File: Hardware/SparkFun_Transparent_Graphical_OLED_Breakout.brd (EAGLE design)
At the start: 25.4 x 25.4 mm, 61 parts, among them U1 AP3012, U2 UG-2856KLBAG01_4WSPI

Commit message: Add capacitor to reset line for delayed start up!
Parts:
- moved U$10 2.54 mm to (11.4, 1.40)
- moved U$11 2.54 mm to (14.0, 1.27)
- moved U$6 2.54 mm to (14.0, 1.40)
- moved U$7 2.54 mm to (11.4, 1.27)
- moved U$12 2.54 mm to (16.5, 1.40)
- moved U$15 2.54 mm to (16.5, 1.27)
- moved U$8 2.54 mm to (19.1, 1.27)
- moved U$9 2.54 mm to (19.1, 1.52)
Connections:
- net !CS: now also J3.6; no longer J3.5
- net D!C!/SA0: now also J3.5; no longer J3.6
- net SCLK/SCL: now also J3.4; no longer J3.3
- net SDIN/SDA: now also J3.3; no longer J3.4
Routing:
- net !CS: track 35.5 -> 32.1 mm, vias 6 -> 5
- net SDIN/SDA: track 64.3 -> 61.8 mm
- net SCLK/SCL: track 59.1 -> 61.6 mm
- net D!C!/SA0: track 32.4 -> 30.1 mm

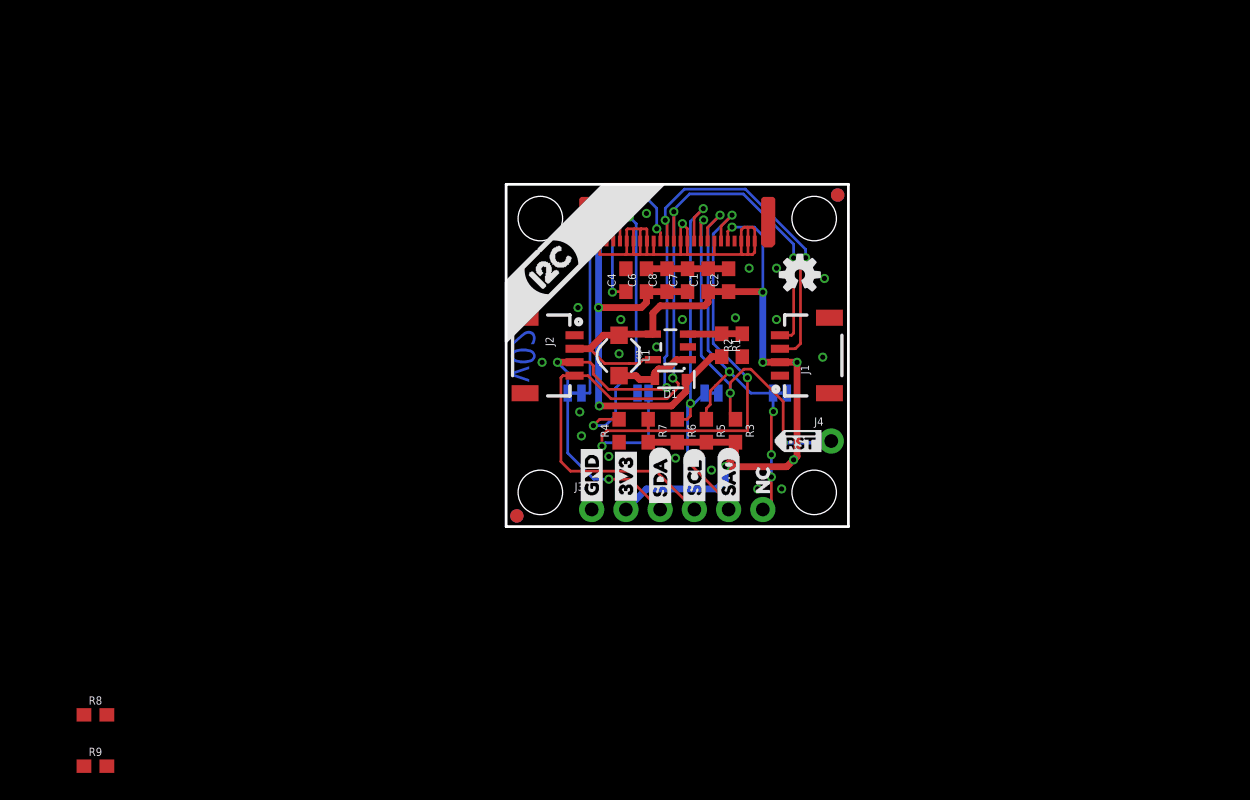
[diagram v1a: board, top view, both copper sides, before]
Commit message: Fixed proto issues
Added I2C pullup resistors and disconnect jumper, added power LED, added reset timing capacitor
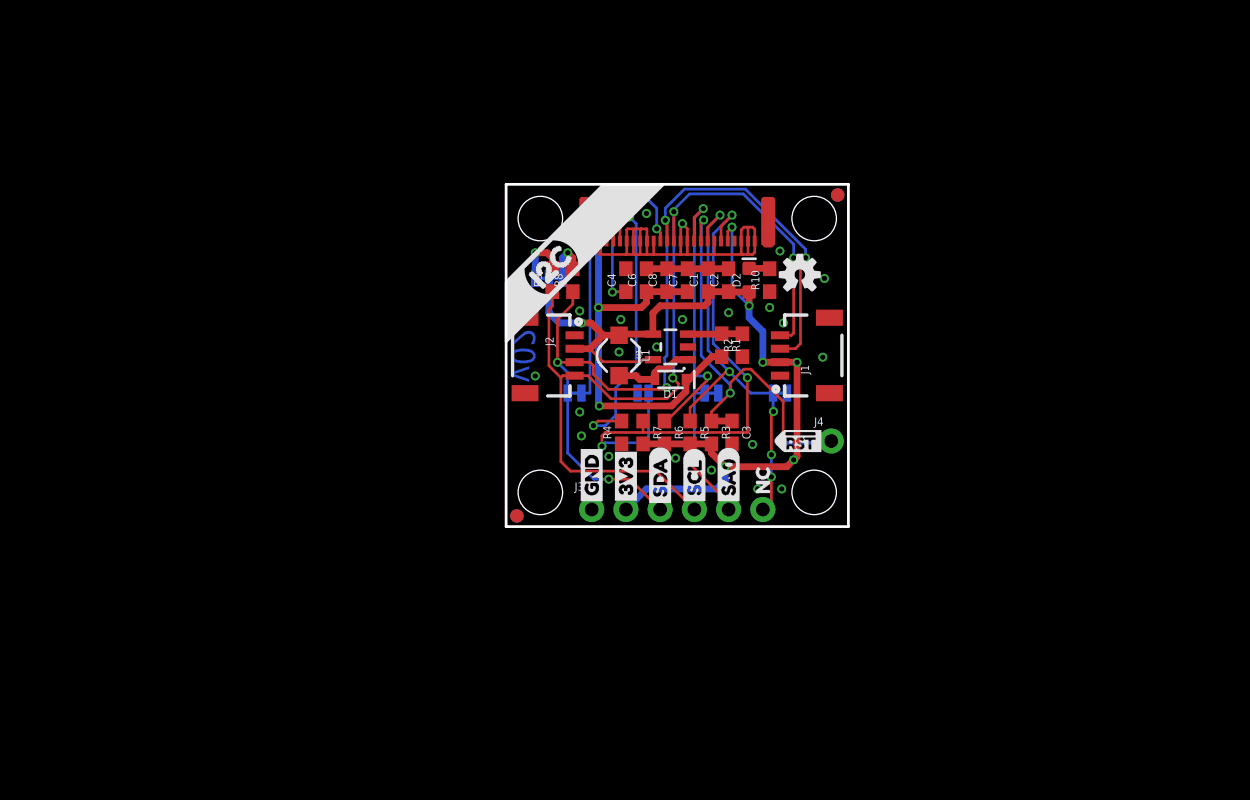
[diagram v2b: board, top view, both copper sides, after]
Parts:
- added C3: 1.0uF, SparkFun-Capacitors:0603
- added D2: RED, SparkFun-LED:LED-0603
- added JP5: I2C PU, SparkFun-Jumpers:SMT-JUMPER_3_2-NC_TRACE_SILK
- added R10: 1k, SparkFun-Resistors:0603
- moved R9 49.5 mm to (3.43, 18.3), turned to 90 degrees
- moved R8 47.9 mm to (4.95, 18.3), turned to 90 degrees
- moved R3 1.78 mm to (15.2, 6.99)
- moved R5 1.21 mm to (13.7, 6.99)
- moved R6 0.96 mm to (11.7, 6.99)
- moved R7 0.40 mm to (10.2, 6.99)
- moved R4 0.23 mm to (8.57, 6.99)
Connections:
- new net N$2: D2.C, R10.2
- new net N$6: JP5.3, R8.2
- new net N$7: JP5.1, R9.2
- net !RES: now also C3.1
- net 3.3V: now also D2.A, JP5.2; no longer R8.2, R9.2
- net GND: now also C3.2, R10.1
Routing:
- net SCLK/SCL: track 61.6 -> 68.5 mm
- net SDIN/SDA: track 61.8 -> 67.5 mm
- net 3.3V: track 68.6 -> 73.3 mm, vias 6 -> 7
- net N$7: track 0.00 -> 4.13 mm, vias 0 -> 1
- net N$6: track 0.00 -> 3.40 mm, vias 0 -> 1
- net D!C!/SA0: track 30.1 -> 33.3 mm
- net !RES: track 30.4 -> 32.4 mm
- net N$2: track 0.00 -> 1.54 mm
- net !CS: track 32.1 -> 32.8 mm
- net GND: vias 22 -> 23

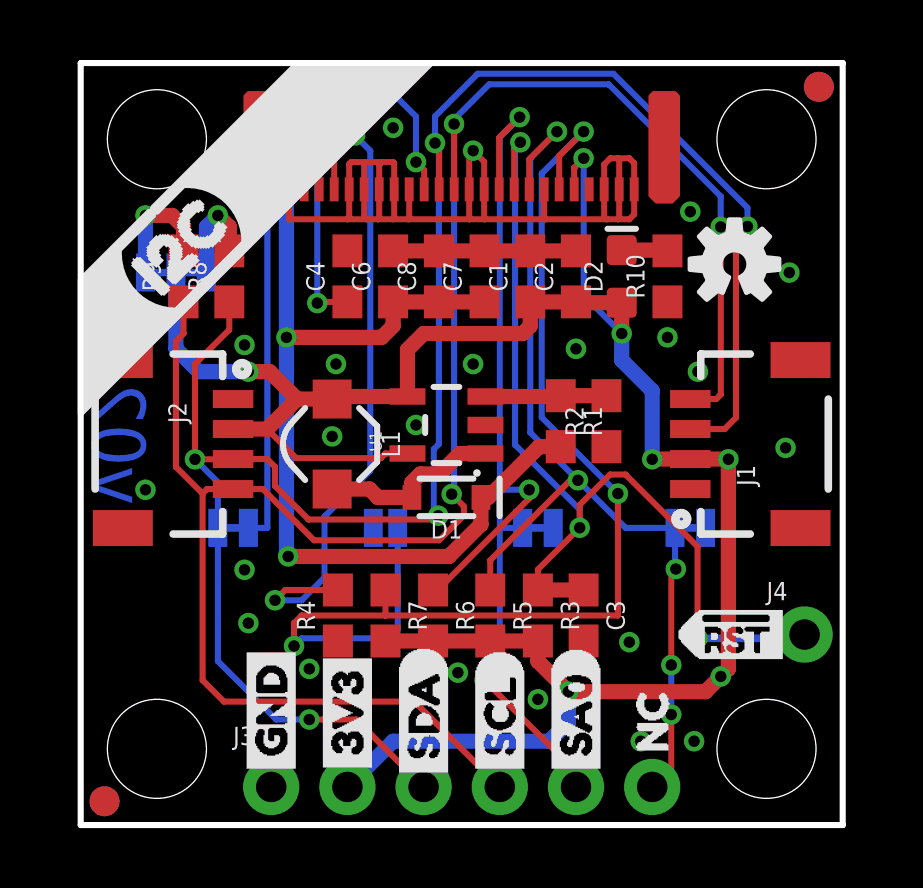
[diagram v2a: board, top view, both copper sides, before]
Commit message: Add label for I2C pullup disconnect jumper
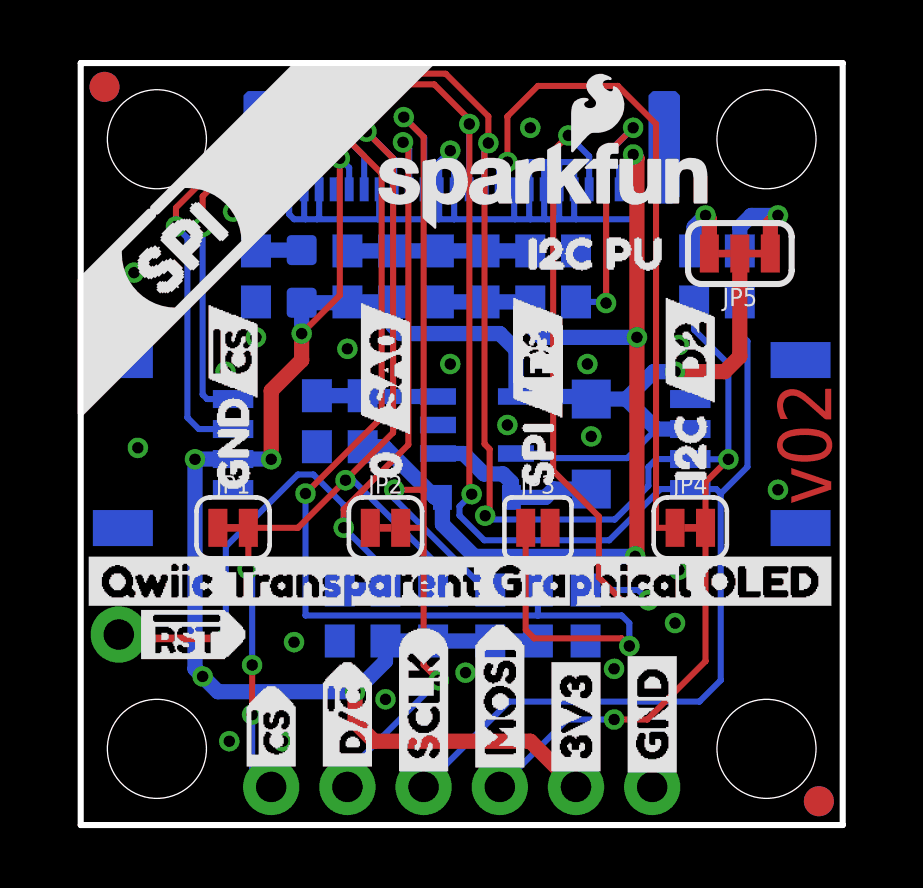
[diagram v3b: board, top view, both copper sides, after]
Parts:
- added U$25: (no value), buzzard_labels:I2C_PU0
- moved FRAME1 48.3 mm to (36.8, -10.2), flipped to the bottom
- moved U$2 25.9 mm to (-0.25, 8.13), flipped to the top
- moved FD1 23.8 mm to (24.6, 0.79), flipped to the bottom
- moved FD2 23.8 mm to (24.6, 0.79), flipped to the top
- moved FD3 23.8 mm to (0.79, 24.6), flipped to the bottom
- moved FD4 23.8 mm to (0.79, 24.6), flipped to the top
- moved U$19 23.1 mm to (24.3, 17.1), flipped to the bottom
- moved J4 22.9 mm to (1.27, 6.35), flipped to the bottom
- moved U$24 22.9 mm to (1.27, 17.1), flipped to the top
- moved U$17 22.7 mm to (1.37, 6.35), flipped to the top
- moved JP5 18.8 mm to (22.0, 19.1), flipped to the top
- moved R9 18.5 mm to (22.0, 18.3), flipped to the bottom
- moved LOGO2 18.2 mm to (3.61, 18.7), flipped to the bottom
- moved R8 15.5 mm to (20.4, 18.3), flipped to the bottom
- moved J1 15.2 mm to (5.08, 12.7), flipped to the bottom
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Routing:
- net N$6: track 3.40 -> 2.66 mm
- net N$7: track 4.13 -> 3.60 mm
- net 3.3V: track 73.3 -> 73.9 mm

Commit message: Tidy schematic
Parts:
- moved FRAME1 48.3 mm to (-11.4, -10.2), flipped to the top
- moved U$2 25.9 mm to (25.7, 8.13), flipped to the bottom
- moved FD1 23.8 mm to (0.79, 0.79), flipped to the top
- moved FD2 23.8 mm to (0.79, 0.79), flipped to the bottom
- moved FD3 23.8 mm to (24.6, 24.6), flipped to the top
- moved FD4 23.8 mm to (24.6, 24.6), flipped to the bottom
- moved U$19 23.1 mm to (1.14, 17.1), flipped to the top
- moved J4 22.9 mm to (24.1, 6.35), flipped to the top
- moved U$24 22.9 mm to (24.1, 17.1), flipped to the bottom
- moved U$17 22.7 mm to (24.0, 6.35), flipped to the bottom
- moved JP5 18.5 mm to (3.43, 19.1), flipped to the bottom
- moved R9 18.5 mm to (3.43, 18.3), flipped to the top
- moved LOGO2 18.2 mm to (21.8, 18.7), flipped to the top
- moved R8 15.5 mm to (4.95, 18.3), flipped to the top
- moved J1 15.2 mm to (20.3, 12.7), flipped to the top
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
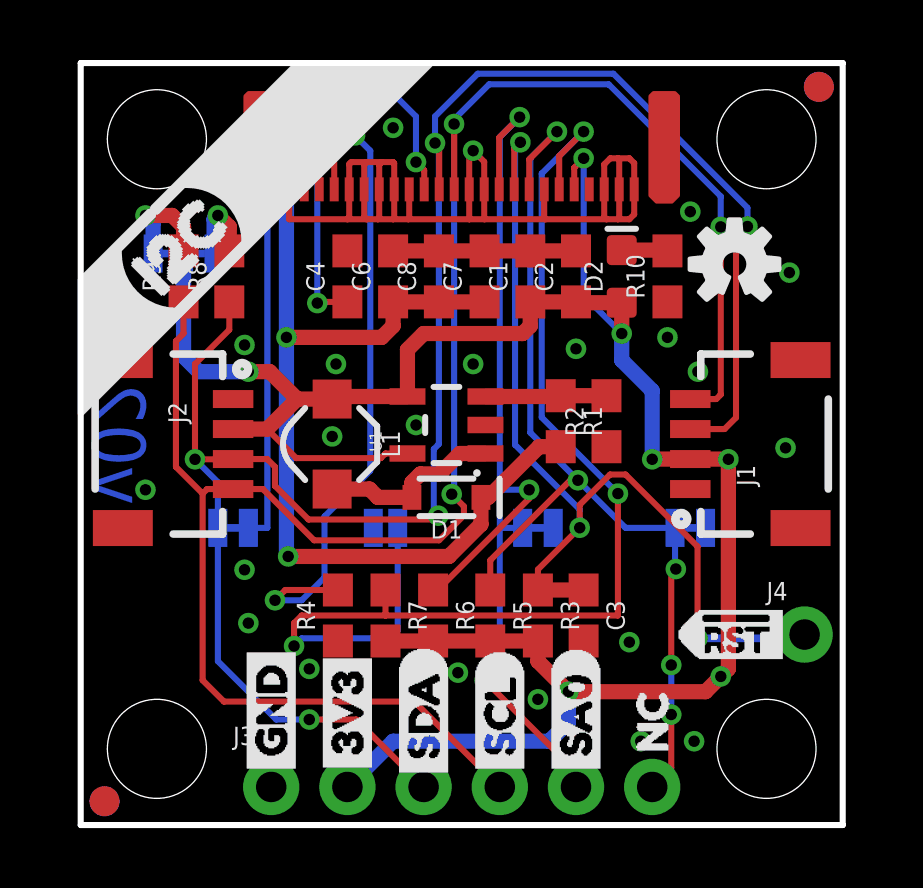
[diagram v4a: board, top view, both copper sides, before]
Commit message: Changed polarity of IFS jumper so that changing to SPI is all cutting, changed silk to match
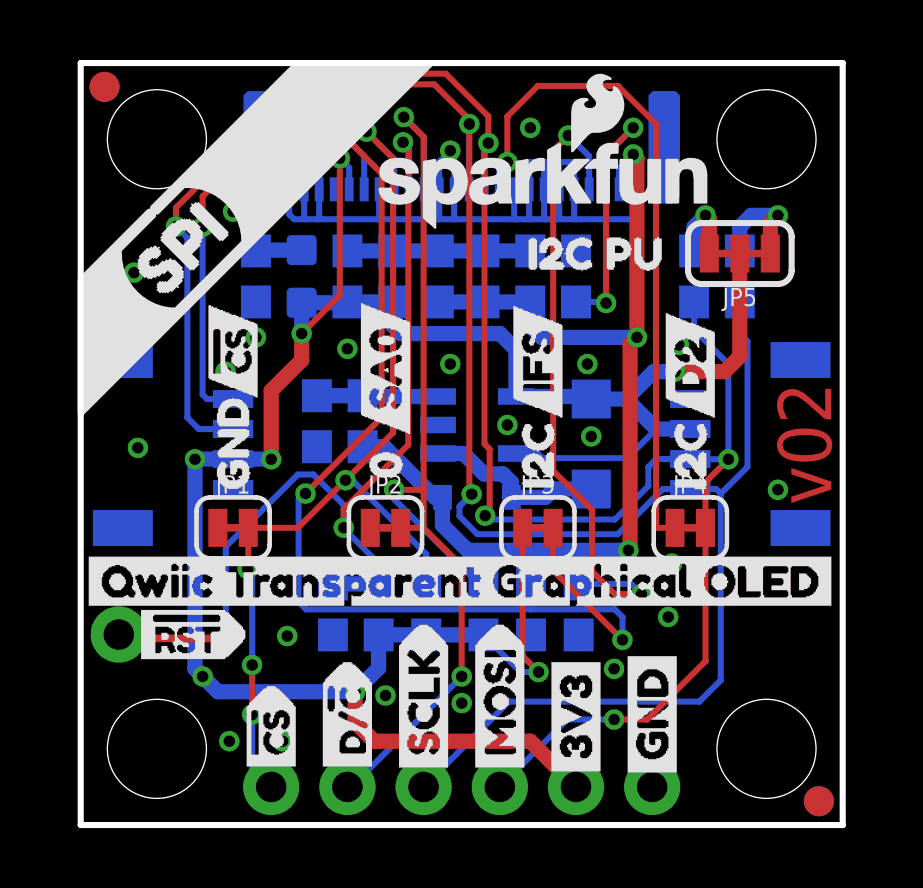
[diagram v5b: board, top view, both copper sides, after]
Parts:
- removed U$29: (no value), buzzard_labels_1:SPI6
- JP3: device SparkFun-Jumpers:SMT-JUMPER_2_NO_SILK -> SparkFun-Jumpers:SMT-JUMPER_2_NC_TRACE_SILK
- U$11: device buzzard_labels:SCLK8 -> buzzard_labels:I2C13
- U$20: device buzzard_labels_1:D27 -> buzzard_labels:SCLK2
- U$6: device buzzard_labels:SCL2 -> buzzard_labels:SCL0
- moved FRAME1 48.3 mm to (36.8, -10.2), flipped to the bottom
- moved U$2 25.9 mm to (-0.25, 8.13), flipped to the top
- moved FD1 23.8 mm to (24.6, 0.79), flipped to the bottom
- moved FD2 23.8 mm to (24.6, 0.79), flipped to the top
- moved FD3 23.8 mm to (0.79, 24.6), flipped to the bottom
- moved FD4 23.8 mm to (0.79, 24.6), flipped to the top
- moved U$19 23.1 mm to (24.3, 17.1), flipped to the bottom
- moved J4 22.9 mm to (1.27, 6.35), flipped to the bottom
- moved U$24 22.9 mm to (1.27, 17.1), flipped to the top
- moved U$17 22.7 mm to (1.37, 6.35), flipped to the top
- moved LOGO2 19.3 mm to (2.46, 18.4), flipped to the bottom
- moved JP5 18.5 mm to (22.0, 19.1), flipped to the top
- moved R9 18.5 mm to (22.0, 18.3), flipped to the bottom
- moved R8 15.5 mm to (20.4, 18.3), flipped to the bottom
- moved U$3 15.2 mm to (20.3, 13.5), flipped to the top
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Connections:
- net 3.3V: now also JP3.1; no longer R7.2
- net GND: now also R7.1; no longer JP3.2
- net I2C!4WSPI: now also JP3.2, R7.2; no longer JP3.1, R7.1
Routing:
- net 3.3V: track 73.9 -> 79.8 mm, vias 7 -> 8
- net I2C!4WSPI: track 39.6 -> 36.1 mm

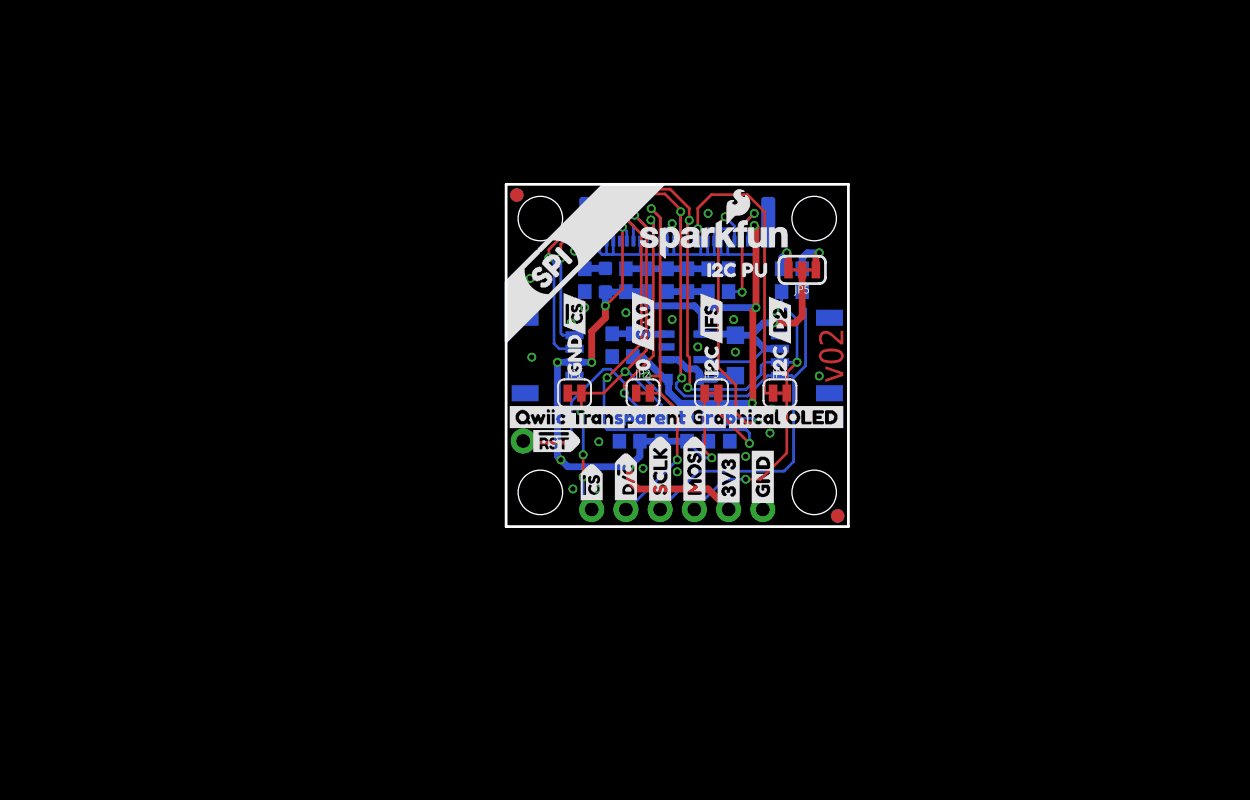
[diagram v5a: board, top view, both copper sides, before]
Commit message: Notes from reds review added in board
Yeah its not standard, but it worked
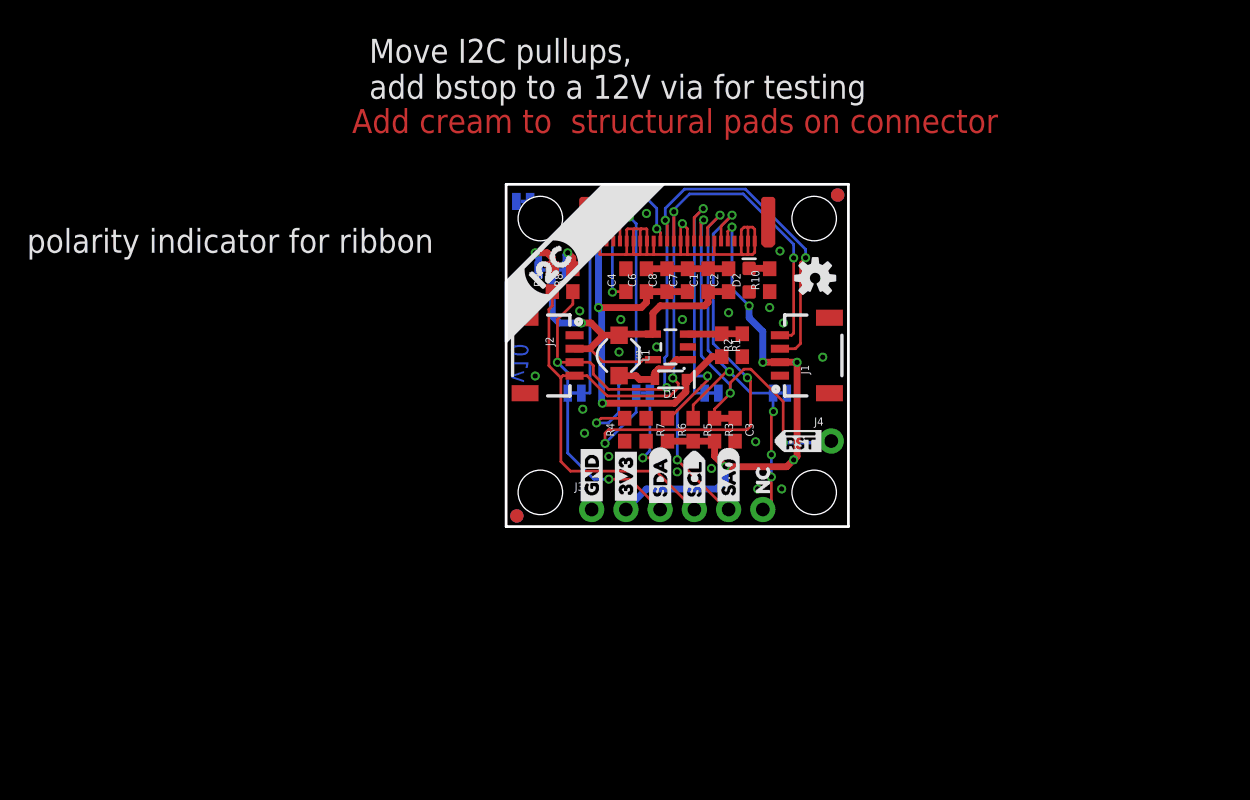
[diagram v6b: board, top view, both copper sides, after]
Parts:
- added JP6: PWR, SparkFun-Jumpers:SMT-JUMPER_2_NC_TRACE_SILK
- moved FRAME1 48.3 mm to (-11.4, -10.2), flipped to the top
- moved U$2 25.9 mm to (25.7, 8.13), flipped to the bottom
- moved FD1 23.8 mm to (0.79, 0.79), flipped to the top
- moved FD2 23.8 mm to (0.79, 0.79), flipped to the bottom
- moved FD3 23.8 mm to (24.6, 24.6), flipped to the top
- moved FD4 23.8 mm to (24.6, 24.6), flipped to the bottom
- moved U$19 23.1 mm to (1.14, 17.1), flipped to the top
- moved J4 22.9 mm to (24.1, 6.35), flipped to the top
- moved U$24 22.9 mm to (24.1, 17.1), flipped to the bottom
- moved U$17 22.7 mm to (24.0, 6.35), flipped to the bottom
- moved LOGO2 20.5 mm to (22.9, 18.4), flipped to the top
- moved JP5 18.5 mm to (3.43, 19.1), flipped to the bottom
- moved R9 18.5 mm to (3.43, 18.3), flipped to the top
- moved R8 15.5 mm to (4.95, 18.3), flipped to the top
- moved J1 15.2 mm to (20.3, 12.7), flipped to the top
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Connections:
- net !RES renamed !RST
- net I2C!4WSPI renamed !4WSPI!/I2C
- new net N$8: D2.A, JP6.1
- net 3.3V: now also JP6.2; no longer D2.A
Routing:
- net 3.3V: track 79.8 -> 77.2 mm
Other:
- board text added: "Add cream to structural pads on connector"
- board text added: "Jumper labels fix (simplify)"
- board text added: "Move I2C pullups, add bstop to a 12V via for testing"
- board text added: "Use JP4, JP3, JP2, JP1"
- board text added: "Version number update"
- board text added: "polarity indicator for ribbon"
- board text added: "v10"
- board text removed: "v02"
